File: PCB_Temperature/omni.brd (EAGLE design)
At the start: 70 x 53.6 mm, 12 parts

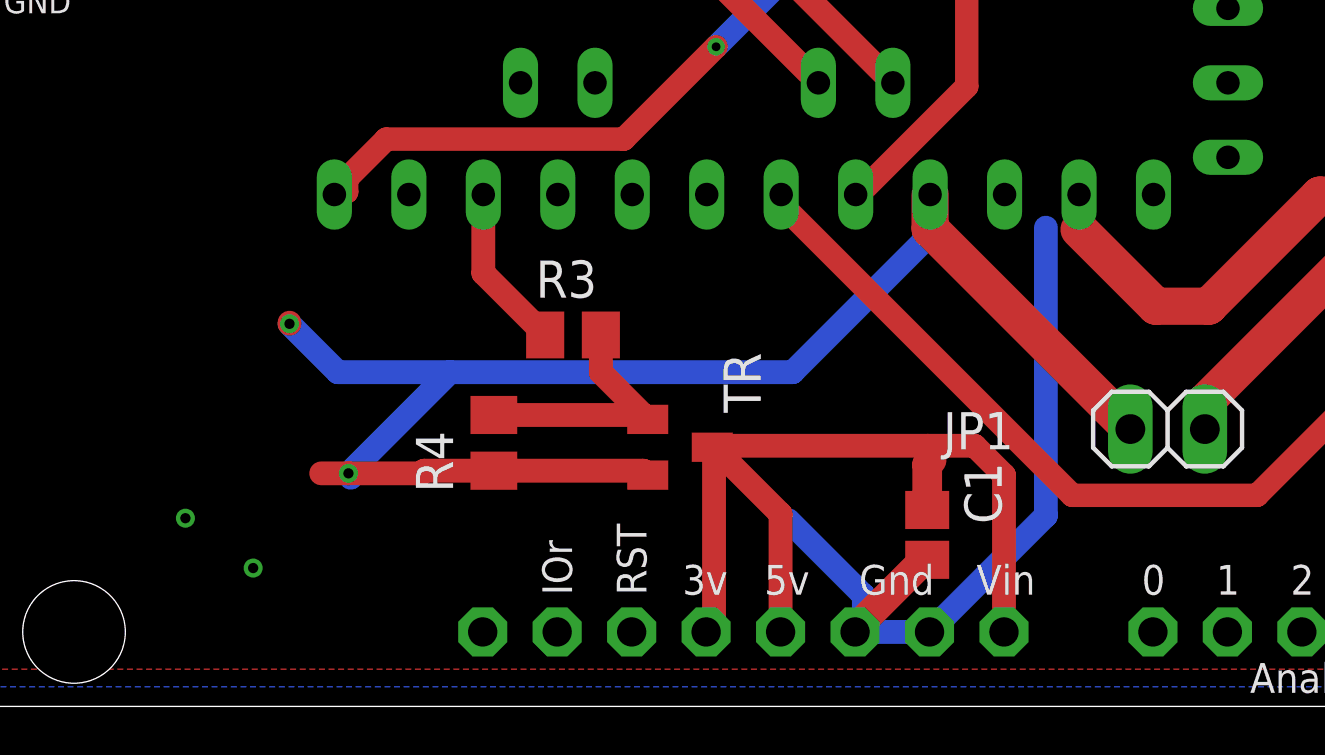
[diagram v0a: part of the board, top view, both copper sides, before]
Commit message: Revise powersource for LoRa
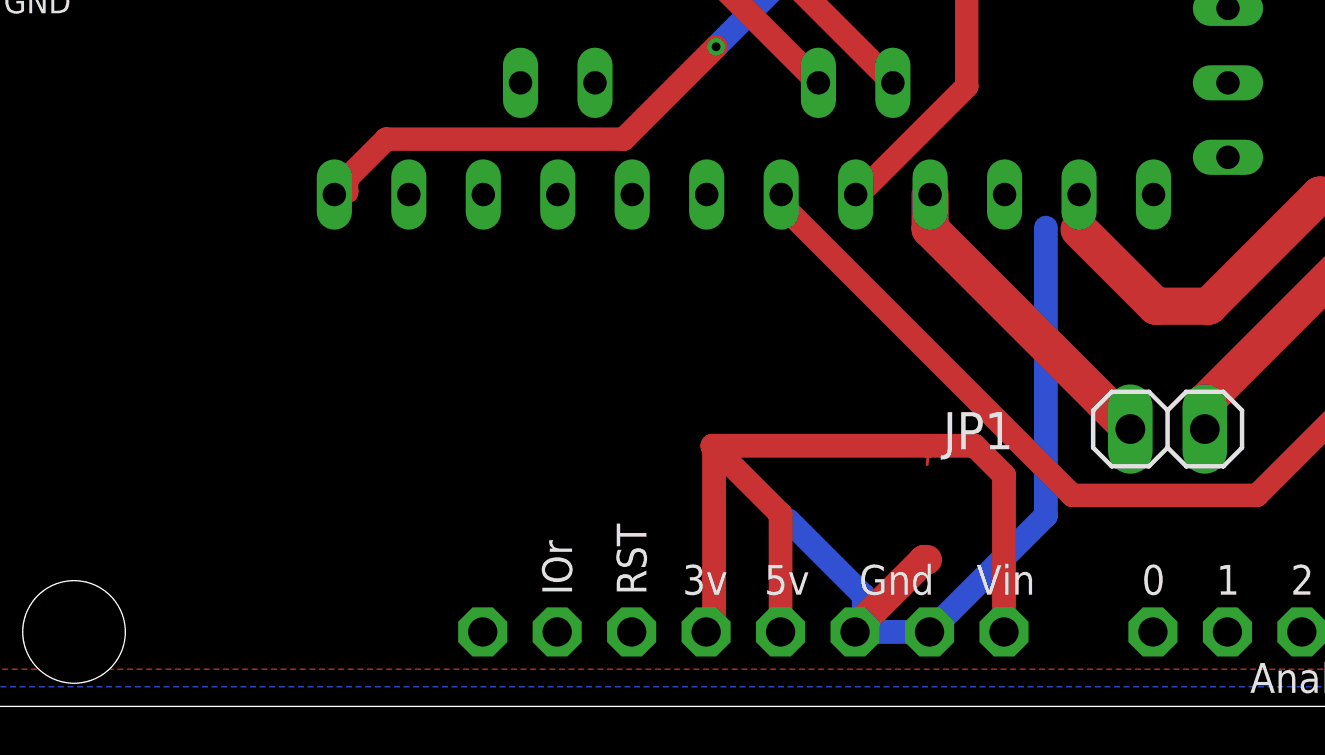
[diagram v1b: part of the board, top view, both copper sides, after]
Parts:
- removed C1: 1uF, rcl:C2012
- removed R3: 430, rcl:M2012
- removed R4: 10K, rcl:M2012
- removed TR: 2SA1298, transistor-pnp:SOT23-BEC
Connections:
- removed net N$5: R3.1, U$1.D12
- removed net N$7: R3.2, R4.2, TR.B
- net GND: no longer C1.2
- net N$4: no longer C1.1, TR.C
- net V+: no longer R4.1, TR.E
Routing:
- net V+: track 53.1 -> 10.8 mm, vias 2 -> 0
- net N$7: track 8.85 -> 0.00 mm
- net N$5: track 5.66 -> 0.00 mm
- net N$4: track 31.9 -> 30.1 mm
- net GND: vias 7 -> 4
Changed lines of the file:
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@@
 <attribute name="VALUE" x="49.76" y="6.285" size="1.27" layer="27"/>
-</element>
-<element name="R3" library="rcl" library_urn="urn:adsk.eagle:library:334" package="M2012" package3d_urn="urn:adsk.eagle:package:23561/1" value="430" x="32.02" y="12.67" smashed="yes">
-<attribute name="NAME" x="30.75" y="13.94" size="1.27" layer="25"/>
-<attribute name="SPICEPREFIX" value="R" x="76.47" y="-76.23" size="1.778" layer="27" display="off"/>
-<attribute name="VALUE" x="30.75" y="10.13" size="1.27" layer="27"/>
-</element>
-<element name="R4" library="rcl" library_urn="urn:adsk.eagle:library:334" package="M2012" package3d_urn="urn:adsk.eagle:package:23561/1" value="10K" x="29.32" y="8.99" smashed="yes" rot="R90">
-<attribute name="NAME" x="27.93" y="7.3" size="1.27" layer="25" rot="R90"/>
-<attribute name="SPICEPREFIX" value="R" x="118.22" y="58.52" size="1.778" layer="27" rot="R90" display="off"/>
-<attribute name="VALUE" x="31.86" y="7.72" size="1.27" layer="27" rot="R90"/>
 </element>
 <element name="U$1" library="Arduino-clone" package="PRO-MINI-2" value="PRO-MINI-2" x="39.12" y="23.81" smashed="yes" rot="R270"/>
 <element name="LTE_LORA" library="adafruit" package="ARDUINOR3-BPLACE" value="ARDUINOR3-BPLACE" x="1" y="0" smashed="yes"/>
-<element name="TR" library="transistor-pnp" library_urn="urn:adsk.eagle:library:399" package="SOT23-BEC" package3d_urn="urn:adsk.eagle:package:29219/2" value="2SA1298" x="35.67" y="8.84" smashed="yes" rot="R270">
-<attribute name="NAME" x="37.155" y="12.065" size="1.27" layer="25" rot="R270"/>
-<attribute name="VALUE" x="32.495" y="10.745" size="1.27" layer="27" rot="R270"/>
-</element>
 <element name="GPS" library="OMNI" package="MA05-1" package3d_urn="urn:adsk.eagle:package:8332/1" value="AE-GYSFDMAXB" x="5.14" y="38.56" smashed="yes" rot="R90">
 <attribute name="MF" value="" x="5.14" y="38.56" size="1.778" layer="27" rot="R90" display="off"/>
@@
 <attribute name="NAME" x="61.3047625" y="10.602078125" size="1.27" layer="21"/>
 <attribute name="VALUE" x="62.92" y="11.16" size="1.27" layer="21" rot="R270"/>
-</element>
-<element name="C1" library="rcl" library_urn="urn:adsk.eagle:library:334" package="C2012" package3d_urn="urn:adsk.eagle:package:23625/2" value="1uF" x="44.1" y="5.85" smashed="yes" rot="R270">
-<attribute name="NAME" x="45.37" y="8.32" size="1.27" layer="25" rot="R270"/>
-<attribute name="SPICEPREFIX" value="C" x="44.1" y="5.85" size="1.778" layer="27" rot="R270" display="off"/>
-<attribute name="VALUE" x="41.56" y="7.12" size="1.27" layer="27" rot="R270"/>
 </element>
 <element name="TEMP1" library="con-amp" library_urn="urn:adsk.eagle:library:127" package="10X03MTA" package3d_urn="urn:adsk.eagle:package:8081621/1" value="" x="40.20185" y="42.851703125" smashed="yes" rot="R270">
@@
 </elements>
 <signals>
+<signal name="S$2">
+<via x="2.15391875" y="2.181859375" extent="1-16" drill="0.35"/>
+</signal>
 <signal name="GND">
 <contactref element="LTE_LORA" pad="GND1"/>
@@
 <contactref element="GPS" pad="4"/>
 <contactref element="USB" pad="GND"/>
-<via x="18.8" y="6.42" extent="1-16" drill="0.35"/>
 <wire x1="44.45" y1="2.54" x2="44.18" y2="2.54" width="0.8128" layer="16"/>
 <wire x1="41.94" y1="3.78" x2="39.37" y2="6.35" width="0.8128" layer="16"/>
@@
 <vertex x="0.67" y="0.77"/>
 </polygon>
-<contactref element="C1" pad="2"/>
 <wire x1="44.1" y1="2.62" x2="44.18" y2="2.54" width="1.016" layer="1"/>
 <wire x1="44.1" y1="5" x2="43.9905375" y2="5" width="1.016" layer="1"/>
@@
 <wire x1="44.18" y1="2.54" x2="48.15" y2="6.51" width="0.8128" layer="16"/>
 <via x="9.80694375" y="50.751740625" extent="1-16" drill="0.35"/>
-<via x="21.1099375" y="4.71931875" extent="1-16" drill="0.35"/>
-<via x="2.15391875" y="2.181859375" extent="1-16" drill="0.35"/>
 <via x="62.80911875" y="7.59968125" extent="1-16" drill="0.35"/>
 <via x="66.977259375" y="30.7746375" extent="1-16" drill="0.35"/>
@@
 <contactref element="LTE_LORA" pad="3V"/>
 <wire x1="36.56" y1="2.54" x2="36.83" y2="2.81" width="0.8128" layer="1"/>
-<contactref element="TR" pad="C"/>
 <contactref element="LTE_LORA" pad="VIN"/>
 <contactref element="LTE_LORA" pad="5V"/>
-<wire x1="36.772359375" y1="8.89" x2="36.77" y2="8.84" width="0.8128" layer="1"/>
 <wire x1="36.772359375" y1="8.89" x2="44.125" y2="8.89" width="0.8128" layer="1"/>
 <wire x1="44.125" y1="8.89" x2="45.72" y2="8.89" width="0.8128" layer="1"/>
 <wire x1="45.72" y1="8.89" x2="46.72" y2="7.89" width="0.8128" layer="1"/>
 <wire x1="46.72" y1="7.89" x2="46.72" y2="2.54" width="0.8128" layer="1"/>
-<contactref element="C1" pad="1"/>
-<wire x1="44.1" y1="6.7" x2="44.1" y2="8.25" width="1.016" layer="1"/>
-<wire x1="44.1" y1="8.25" x2="44.25" y2="8.4" width="1.016" layer="1"/>
 <wire x1="36.83" y1="8.832359375" x2="36.772359375" y2="8.89" width="0.8128" layer="1"/>
 <wire x1="36.83" y1="2.81" x2="36.83" y2="8.832359375" width="0.8128" layer="1"/>
@@
 <wire x1="44.125" y1="8.5" x2="44.125" y2="8.89" width="0.1" layer="1"/>
 </signal>
-<signal name="N$7">
-<contactref element="R3" pad="2"/>
-<contactref element="TR" pad="B"/>
-<contactref element="R4" pad="2"/>
-<wire x1="34.57" y1="9.79" x2="32.97" y2="11.39" width="0.8128" layer="1"/>
-<wire x1="32.97" y1="11.39" x2="32.97" y2="12.67" width="0.8128" layer="1"/>
-<wire x1="34.57" y1="9.79" x2="34.42" y2="9.94" width="0.8128" layer="1"/>
-<wire x1="34.42" y1="9.94" x2="29.32" y2="9.94" width="0.8128" layer="1"/>
-</signal>
 <signal name="V+">
 <contactref element="U$1" pad="VCC"/>
 <contactref element="JP1" pad="1"/>
-<via x="24.36" y="7.95" extent="1-16" drill="0.35"/>
-<wire x1="44.2" y1="17.46" x2="44.2" y2="16.09" width="0.8128" layer="16"/>
-<contactref element="TR" pad="E"/>
-<contactref element="R4" pad="1"/>
-<wire x1="34.57" y1="7.89" x2="34.42" y2="8.04" width="0.8128" layer="1"/>
-<wire x1="34.42" y1="8.04" x2="29.32" y2="8.04" width="0.8128" layer="1"/>
-<wire x1="51.03" y1="9.46" x2="44.2" y2="16.29" width="1.27" layer="1"/>
-<wire x1="44.2" y1="16.29" x2="44.2" y2="17.46" width="1.27" layer="1"/>
-<wire x1="44.2" y1="16.09" x2="39.51" y2="11.4" width="0.8128" layer="16"/>
-<wire x1="24.4396" y1="8.0178125" x2="24.4396" y2="7.8" width="0.8128" layer="16"/>
-<wire x1="27.8217875" y1="11.4" x2="24.4396" y2="8.0178125" width="0.8128" layer="16"/>
-<wire x1="39.51" y1="11.4" x2="27.8217875" y2="11.4" width="0.8128" layer="16"/>
-<wire x1="29.32" y1="8.04" x2="26.94" y2="8.04" width="0.8128" layer="1"/>
-<wire x1="26.94" y1="8.04" x2="26.85" y2="7.95" width="0.8128" layer="1"/>
-<wire x1="26.85" y1="7.95" x2="24.36" y2="7.95" width="0.8128" layer="1"/>
-<wire x1="24.36" y1="7.95" x2="23.43" y2="7.95" width="0.8128" layer="1"/>
-<wire x1="27.8217875" y1="11.4" x2="24" y2="11.4" width="0.8128" layer="16"/>
-<wire x1="24" y1="11.4" x2="22.35" y2="13.05" width="0.8128" layer="16"/>
-<via x="22.35" y="13.05" extent="1-16" drill="0.35"/>
-<wire x1="22.35" y1="13.05" x2="22.35" y2="13.08855625" width="0.8128" layer="1"/>
-<wire x1="24.375" y1="8" x2="24.36" y2="7.95" width="0.1" layer="16"/>
-<wire x1="24.375" y1="8" x2="24.4396" y2="8.0178125" width="0.1" layer="16"/>
+<wire x1="44.2" y1="16.29" x2="51.03" y2="9.46" width="1.27" layer="1"/>
+<wire x1="44.2" y1="17.46" x2="44.2" y2="16.29" width="1.27" layer="1"/>
 </signal>
 <signal name="N$1">
@@
 <wire x1="7.21" y1="43.64" x2="5.14" y2="43.64" width="0.8128" layer="1"/>
 </signal>
-<signal name="N$5">
-<contactref element="R3" pad="1"/>
-<contactref element="U$1" pad="D12"/>
-<wire x1="31.07" y1="12.67" x2="28.96" y2="14.78" width="0.8128" layer="1"/>
-<wire x1="28.96" y1="14.78" x2="28.96" y2="17.46" width="0.8128" layer="1"/>
-</signal>
 <signal name="N$12">

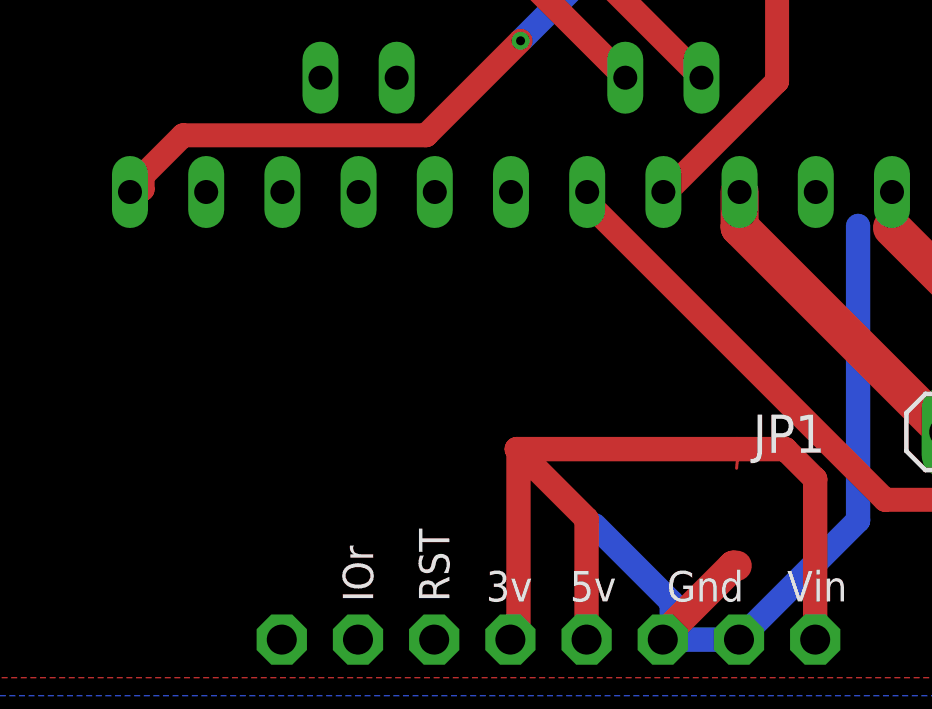
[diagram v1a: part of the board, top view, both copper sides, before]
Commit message: Modify TMP35 board with power saving
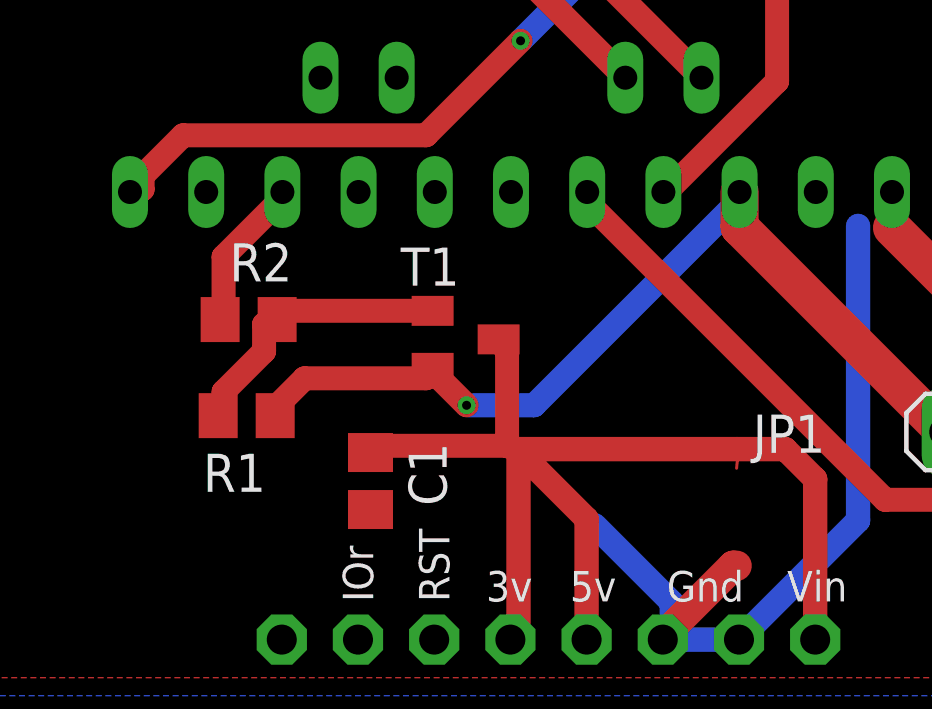
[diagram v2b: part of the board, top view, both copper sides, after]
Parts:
- added C1: (no value), rcl:C0805
- added R1, R2: (no value), rcl:R0805
- added T1: (no value), microchip:SOT23
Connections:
- new net S$1: R1.2, R2.2, T1.1
- new net S$3: R2.1, U$1.D12
- net GND: now also C1.2
- net N$4: now also C1.1, T1.3
- net V+: now also R1.1, T1.2
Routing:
- net V+: track 10.8 -> 30.8 mm, vias 0 -> 1
- net S$1: track 0.00 -> 9.57 mm
- net N$4: track 30.1 -> 38.9 mm
- net S$3: track 0.00 -> 5.05 mm
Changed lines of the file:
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@@
 <layer number="25" name="tNames" color="7" fill="1" visible="yes" active="yes"/>
 <layer number="26" name="bNames" color="7" fill="1" visible="no" active="yes"/>
-<layer number="27" name="tValues" color="7" fill="1" visible="no" active="yes"/>
+<layer number="27" name="tValues" color="7" fill="1" visible="yes" active="yes"/>
 <layer number="28" name="bValues" color="7" fill="1" visible="no" active="yes"/>
 <layer number="29" name="tStop" color="7" fill="3" visible="no" active="yes"/>
@@
 <autorouter>
 <pass name="Default">
-<param name="RoutingGrid" value="0.5mm"/>
+<param name="RoutingGrid" value="0.125mm"/>
 <param name="AutoGrid" value="1"/>
 <param name="Efforts" value="1"/>
@@
 <attribute name="VALUE" x="58.499525" y="46.627903125" size="1.27" layer="27" rot="R270"/>
 </element>
+<element name="T1" library="microchip" library_urn="urn:adsk.eagle:library:294" package="SOT23" package3d_urn="urn:adsk.eagle:package:20834/2" value="" x="35.067240625" y="12.5476" smashed="yes" rot="R270">
+<attribute name="NAME" x="34.858959375" y="15.6083" size="1.27" layer="25" rot="R180"/>
+<attribute name="VALUE" x="31.892240625" y="14.4526" size="1.27" layer="27" rot="R270"/>
+</element>
+<element name="C1" library="rcl" library_urn="urn:adsk.eagle:library:334" package="C0805" package3d_urn="urn:adsk.eagle:package:23617/2" value="" x="31.897321875" y="7.82574375" smashed="yes" rot="R270">
+<attribute name="NAME" x="33.167321875" y="9.09574375" size="1.27" layer="25" rot="R270"/>
+<attribute name="VALUE" x="29.357321875" y="9.09574375" size="1.27" layer="27" rot="R270"/>
+</element>
+<element name="R2" library="rcl" library_urn="urn:adsk.eagle:library:334" package="R0805" package3d_urn="urn:adsk.eagle:package:23553/2" value="" x="27.8358625" y="13.208" smashed="yes">
+<attribute name="NAME" x="27.2008625" y="14.478" size="1.27" layer="25"/>
+<attribute name="VALUE" x="27.2008625" y="10.668" size="1.27" layer="27"/>
+</element>
+<element name="R1" library="rcl" library_urn="urn:adsk.eagle:library:334" package="R0805" package3d_urn="urn:adsk.eagle:package:23553/2" value="" x="27.769821875" y="10.005059375" smashed="yes" rot="R180">
+<attribute name="NAME" x="28.404821875" y="8.735059375" size="1.27" layer="25" rot="R180"/>
+<attribute name="VALUE" x="28.404821875" y="12.545059375" size="1.27" layer="27" rot="R180"/>
+</element>
 </elements>
 <signals>
@@
 <contactref element="TEMP2" pad="1"/>
 <contactref element="TEMP1" pad="1"/>
+<contactref element="C1" pad="2"/>
 </signal>
 <signal name="N$4">
@@
 <wire x1="44.125" y1="8.5" x2="44.1" y2="8.25" width="0.1" layer="1"/>
 <wire x1="44.125" y1="8.5" x2="44.125" y2="8.89" width="0.1" layer="1"/>
+<contactref element="T1" pad="3"/>
+<contactref element="C1" pad="1"/>
+<wire x1="36.45" y1="9" x2="36.45" y2="12.15" width="0.8" layer="1"/>
+<wire x1="36.45" y1="12.15" x2="36.167240625" y2="12.5476" width="0.8" layer="1"/>
+<wire x1="36.45" y1="9" x2="31.95" y2="9" width="0.8" layer="1"/>
+<wire x1="31.95" y1="9" x2="31.897321875" y2="8.77574375" width="0.8" layer="1"/>
+<wire x1="36.45" y1="9" x2="36.83" y2="8.832359375" width="0.8" layer="1"/>
 </signal>
 <signal name="V+">
@@
 <wire x1="44.2" y1="16.29" x2="51.03" y2="9.46" width="1.27" layer="1"/>
 <wire x1="44.2" y1="17.46" x2="44.2" y2="16.29" width="1.27" layer="1"/>
+<contactref element="T1" pad="2"/>
+<contactref element="R1" pad="1"/>
+<wire x1="29.7" y1="11.25" x2="33.75" y2="11.25" width="0.8" layer="1"/>
+<wire x1="28.8" y1="10.35" x2="29.7" y2="11.25" width="0.8" layer="1"/>
+<wire x1="33.75" y1="11.25" x2="33.967240625" y2="11.5976" width="0.8" layer="1"/>
+<wire x1="28.8" y1="10.35" x2="28.719821875" y2="10.005059375" width="0.8" layer="1"/>
+<wire x1="35.1" y1="10.35" x2="34.2" y2="11.25" width="0.8" layer="1"/>
+<wire x1="37.35" y1="10.35" x2="35.1" y2="10.35" width="0.8" layer="16"/>
+<wire x1="44.1" y1="17.1" x2="37.35" y2="10.35" width="0.8" layer="16"/>
+<wire x1="34.2" y1="11.25" x2="33.967240625" y2="11.5976" width="0.8" layer="1"/>
+<wire x1="44.1" y1="17.1" x2="44.2" y2="17.46" width="0.8" layer="16"/>
+<via x="35.1" y="10.35" extent="1-16" drill="0.3"/>
 </signal>
 <signal name="N$1">
@@
 <wire x1="56.348625" y1="45.391703125" x2="48.2752375" y2="45.391703125" width="0.8128" layer="1"/>
 </signal>
+<signal name="S$1">
+<contactref element="R1" pad="2"/>
+<contactref element="T1" pad="1"/>
+<contactref element="R2" pad="2"/>
+<wire x1="28.8" y1="13.5" x2="33.75" y2="13.5" width="0.8" layer="1"/>
+<wire x1="33.75" y1="13.5" x2="33.967240625" y2="13.4976" width="0.8" layer="1"/>
+<wire x1="28.8" y1="13.5" x2="28.7858625" y2="13.208" width="0.8" layer="1"/>
+<wire x1="27" y1="10.8" x2="27" y2="10.35" width="0.8" layer="1"/>
+<wire x1="28.35" y1="12.15" x2="27" y2="10.8" width="0.8" layer="1"/>
+<wire x1="28.35" y1="13.05" x2="28.35" y2="12.15" width="0.8" layer="1"/>
+<wire x1="27" y1="10.35" x2="26.819821875" y2="10.005059375" width="0.8" layer="1"/>
+<wire x1="28.35" y1="13.05" x2="28.7858625" y2="13.208" width="0.8" layer="1"/>
+</signal>
+<signal name="S$3">
+<contactref element="U$1" pad="D12"/>
+<contactref element="R2" pad="1"/>
+<wire x1="27" y1="15.3" x2="27" y2="13.5" width="0.8" layer="1"/>
+<wire x1="28.8" y1="17.1" x2="27" y2="15.3" width="0.8" layer="1"/>
+<wire x1="27" y1="13.5" x2="26.8858625" y2="13.208" width="0.8" layer="1"/>
+<wire x1="28.8" y1="17.1" x2="28.96" y2="17.46" width="0.8" layer="1"/>
+</signal>
 </signals>
